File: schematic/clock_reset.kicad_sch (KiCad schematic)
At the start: 39 parts, among them Q2 2N3906, U22 74LS04, U7 74LS05, U8 74LS74, Y1 7.159090Mhz

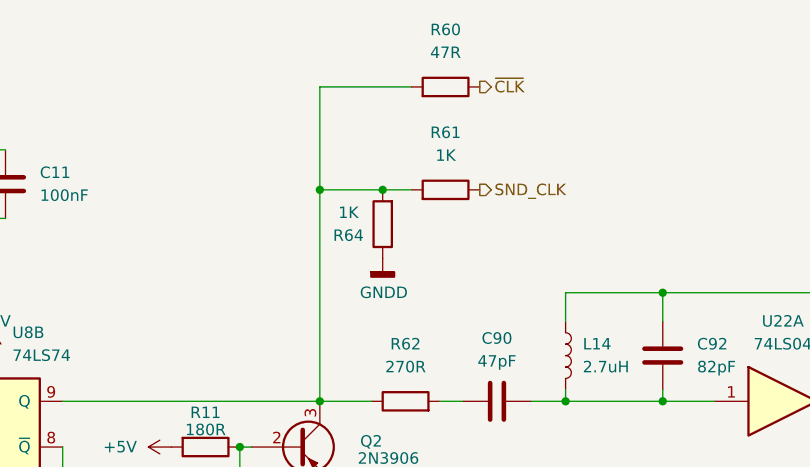
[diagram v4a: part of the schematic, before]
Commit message: added video memory connections
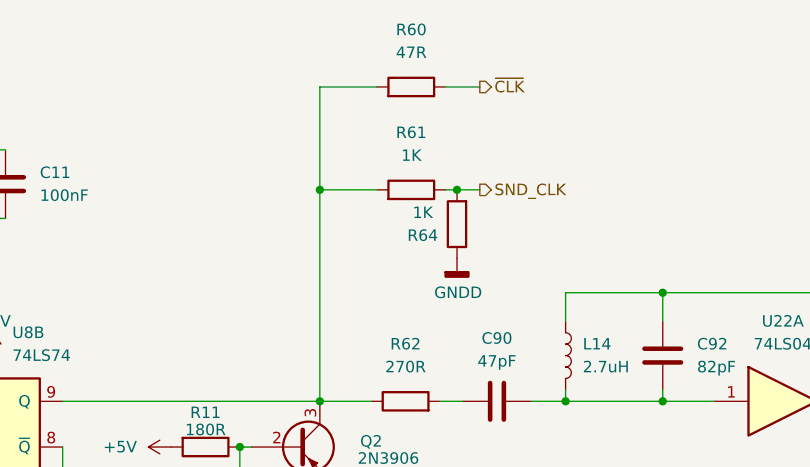
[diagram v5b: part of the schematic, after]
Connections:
- net SND_CLK: now also R64.2
- net at Q2.3 (C), R60.2, R61.2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: no longer R64.2
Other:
- moved on the sheet: R60, R61, R64
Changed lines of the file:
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@@
   (junction (at 73.025 167.64) (diameter 0) (color 0 0 0 0)
   )
-  (junction (at 171.45 40.005) (diameter 0) (color 0 0 0 0)
-  )
   (junction (at 164.465 63.5) (diameter 0) (color 0 0 0 0)
   )
@@
   (junction (at 102.235 158.75) (diameter 0) (color 0 0 0 0)
   )
+  (junction (at 179.705 40.005) (diameter 0) (color 0 0 0 0)
+  )
   (junction (at 80.645 86.36) (diameter 0) (color 0 0 0 0)
   )
@@
     (stroke (width 0) (type default) (color 0 0 0 0))
   )
+  (wire (pts (xy 182.245 40.005) (xy 179.705 40.005))
+    (stroke (width 0) (type default) (color 0 0 0 0))
+  )
   (wire (pts (xy 57.15 74.93) (xy 53.34 74.93))
     (stroke (width 0) (type default) (color 0 0 0 0))
@@
     (stroke (width 0) (type default) (color 0 0 0 0))
   )
+  (wire (pts (xy 178.435 28.575) (xy 182.245 28.575))
+    (stroke (width 0) (type default) (color 0 0 0 0))
+  )
   (wire (pts (xy 60.96 86.36) (xy 60.96 78.74))
     (stroke (width 0) (type default) (color 0 0 0 0))
@@
     (stroke (width 0) (type default) (color 0 0 0 0))
   )
+  (wire (pts (xy 179.705 40.005) (xy 178.435 40.005))
+    (stroke (width 0) (type default) (color 0 0 0 0))
+  )
   (wire (pts (xy 80.645 74.93) (xy 80.645 86.36))
     (stroke (width 0) (type default) (color 0 0 0 0))
@@
     (stroke (width 0) (type default) (color 0 0 0 0))
   )
-  (wire (pts (xy 171.45 40.005) (xy 164.465 40.005))
-    (stroke (width 0) (type default) (color 0 0 0 0))
-  )
   (wire (pts (xy 155.575 68.58) (xy 156.845 68.58))
     (stroke (width 0) (type default) (color 0 0 0 0))
@@
     (stroke (width 0) (type default) (color 0 0 0 0))
   )
-  (wire (pts (xy 164.465 28.575) (xy 174.625 28.575))
+  (wire (pts (xy 164.465 28.575) (xy 170.815 28.575))
     (stroke (width 0) (type default) (color 0 0 0 0))
   )
@@
     (stroke (width 0) (type default) (color 0 0 0 0))
   )
-  (wire (pts (xy 174.625 40.005) (xy 171.45 40.005))
+  (wire (pts (xy 164.465 40.005) (xy 170.815 40.005))
     (stroke (width 0) (type default) (color 0 0 0 0))
   )
@@
     (pin "2")
   )
-  (symbol (lib_id "power:GNDD") (at 171.45 47.625 0) (unit 1)
-    (in_bom yes) (on_board yes)
-    (property "Reference" "#PWR0180" (id 0) (at 171.45 53.975 0)
-      (effects (font (size 1.27 1.27)) hide)
-    )
-    (property "Value" "GNDD" (id 1) (at 168.91 51.435 0)
-      (effects (font (size 1.27 1.27)) (justify left))
-    )
-    (property "Footprint" "" (id 2) (at 171.45 47.625 0)
-      (effects (font (size 1.27 1.27)) hide)
-    )
-    (property "Datasheet" "" (id 3) (at 171.45 47.625 0)
+  (symbol (lib_id "power:GNDD") (at 179.705 47.625 0) (unit 1)
+    (in_bom yes) (on_board yes)
+    (property "Reference" "#PWR0180" (id 0) (at 179.705 53.975 0)
+      (effects (font (size 1.27 1.27)) hide)
+    )
+    (property "Value" "GNDD" (id 1) (at 177.165 51.435 0)
+      (effects (font (size 1.27 1.27)) (justify left))
+    )
+    (property "Footprint" "" (id 2) (at 179.705 47.625 0)
+      (effects (font (size 1.27 1.27)) hide)
+    )
+    (property "Datasheet" "" (id 3) (at 179.705 47.625 0)
       (effects (font (size 1.27 1.27)) hide)
     )
@@
     (pin "7")
   )
-  (symbol (lib_id "Device:R") (at 178.435 28.575 270) (mirror x) (unit 1)
-    (in_bom yes) (on_board yes) (fields_autoplaced)
-    (property "Reference" "R60" (id 0) (at 178.435 22.225 90))
-    (property "Value" "47R" (id 1) (at 178.435 24.765 90))
-    (property "Footprint" "Resistor_THT:R_Axial_DIN0207_L6.3mm_D2.5mm_P10.16mm_Horizontal" (id 2) (at 178.435 30.353 90)
-      (effects (font (size 1.27 1.27)) hide)
-    )
-    (property "Datasheet" "~" (id 3) (at 178.435 28.575 0)
+  (symbol (lib_id "Device:R") (at 174.625 28.575 270) (mirror x) (unit 1)
+    (in_bom yes) (on_board yes) (fields_autoplaced)
+    (property "Reference" "R60" (id 0) (at 174.625 22.225 90))
+    (property "Value" "47R" (id 1) (at 174.625 24.765 90))
+    (property "Footprint" "Resistor_THT:R_Axial_DIN0207_L6.3mm_D2.5mm_P10.16mm_Horizontal" (id 2) (at 174.625 30.353 90)
+      (effects (font (size 1.27 1.27)) hide)
+    )
+    (property "Datasheet" "~" (id 3) (at 174.625 28.575 0)
       (effects (font (size 1.27 1.27)) hide)
     )
@@
     (pin "1")
   )
-  (symbol (lib_id "Device:R") (at 171.45 43.815 180) (unit 1)
-    (in_bom yes) (on_board yes)
-    (property "Reference" "R64" (id 0) (at 167.64 45.085 0))
-    (property "Value" "1K" (id 1) (at 167.64 42.545 0))
-    (property "Footprint" "Resistor_THT:R_Axial_DIN0207_L6.3mm_D2.5mm_P10.16mm_Horizontal" (id 2) (at 173.228 43.815 90)
-      (effects (font (size 1.27 1.27)) hide)
-    )
-    (property "Datasheet" "~" (id 3) (at 171.45 43.815 0)
+  (symbol (lib_id "Device:R") (at 179.705 43.815 180) (unit 1)
+    (in_bom yes) (on_board yes)
+    (property "Reference" "R64" (id 0) (at 175.895 45.085 0))
+    (property "Value" "1K" (id 1) (at 175.895 42.545 0))
+    (property "Footprint" "Resistor_THT:R_Axial_DIN0207_L6.3mm_D2.5mm_P10.16mm_Horizontal" (id 2) (at 181.483 43.815 90)
+      (effects (font (size 1.27 1.27)) hide)
+    )
+    (property "Datasheet" "~" (id 3) (at 179.705 43.815 0)
       (effects (font (size 1.27 1.27)) hide)
     )
@@
     (pin "2")
   )
-  (symbol (lib_id "Device:R") (at 178.435 40.005 270) (mirror x) (unit 1)
-    (in_bom yes) (on_board yes) (fields_autoplaced)
-    (property "Reference" "R61" (id 0) (at 178.435 33.655 90))
-    (property "Value" "1K" (id 1) (at 178.435 36.195 90))
-    (property "Footprint" "Resistor_THT:R_Axial_DIN0207_L6.3mm_D2.5mm_P10.16mm_Horizontal" (id 2) (at 178.435 41.783 90)
-      (effects (font (size 1.27 1.27)) hide)
-    )
-    (property "Datasheet" "~" (id 3) (at 178.435 40.005 0)
-      (effects (font (size 1.27 1.27)) hide)
-    )
+  (symbol (lib_id "Device:R") (at 174.625 40.005 270) (mirror x) (unit 1)
+    (in_bom yes) (on_board yes) (fields_autoplaced)
+    (property "Reference" "R61" (id 0) (at 174.625 33.655 90))
+    (property "Value" "1K" (id 1) (at 174.625 36.195 90))
+    (property "Footprint" "Resistor_THT:R_Axial_DIN0207_L6.3mm_D2.5mm_P10.16mm_Horizontal" (id 2) (at 174.625 41.783 90)
+      (effects (font (size 1.27 1.27)) hide)
+    )
+    (property "Datasheet" "~" (id 3) (at 174.625 40.005 0)
+      (effects (font (size 1.27 1.27)) hide)
+    )

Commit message: added memory, eprom and sound lines. some video as well. fixed the cap size for polar. its a bit weird since they use 5 mm pin and 5mm body and bend out the leads.
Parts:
- C3: footprint Capacitor_THT:CP_Radial_D5.0mm_P2.50mm -> Capacitor_THT:CP_Radial_Tantal_D4.5mm_P5.00mm
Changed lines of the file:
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@@
     (property "Reference" "C3" (id 0) (at 62.865 174.625 0))
     (property "Value" "10uF" (id 1) (at 62.865 176.53 0))
-    (property "Footprint" "Capacitor_THT:CP_Radial_D5.0mm_P2.50mm" (id 2) (at 68.9102 179.07 0)
+    (property "Footprint" "Capacitor_THT:CP_Radial_Tantal_D4.5mm_P5.00mm" (id 2) (at 68.9102 179.07 0)
       (effects (font (size 1.27 1.27)) hide)
     )

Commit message: added new models, fixed the drc errors. changed power width.
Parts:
- C3: footprint Capacitor_THT:CP_Radial_Tantal_D4.5mm_P5.00mm -> Capacitor_THT:CP_Radial_D8.0mm_P5.00mm
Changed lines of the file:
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@@
     (property "Reference" "C3" (id 0) (at 62.865 174.625 0))
     (property "Value" "10uF" (id 1) (at 62.865 176.53 0))
-    (property "Footprint" "Capacitor_THT:CP_Radial_Tantal_D4.5mm_P5.00mm" (id 2) (at 68.9102 179.07 0)
+    (property "Footprint" "Capacitor_THT:CP_Radial_D8.0mm_P5.00mm" (id 2) (at 68.9102 179.07 0)
       (effects (font (size 1.27 1.27)) hide)
     )

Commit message: updated schematic with new layout
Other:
- company: (none) -> sparkletron
- title: Colecovision Schematic -> Reverse Engineer Colecovision
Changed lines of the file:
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@@
   (paper "USLetter")
   (title_block
-    (title "Colecovision Schematic")
-    (date "2023-01-09")
-    (rev "F.0")
+    (title "Reverse Engineer Colecovision")
+    (date "2023-03-14")
+    (rev "DEV")
+    (company "sparkletron")
     (comment 1 "Jay Convertino")
+    (comment 2 "MIT LICENSE")
   )
   (junction (at 179.07 127.635) (diameter 0) (color 0 0 0 0)
